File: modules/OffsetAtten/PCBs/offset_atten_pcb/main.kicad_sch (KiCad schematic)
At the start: 25 parts, among them J9 Eurorack_2x5_Power, U1 LM324, U2 LM324

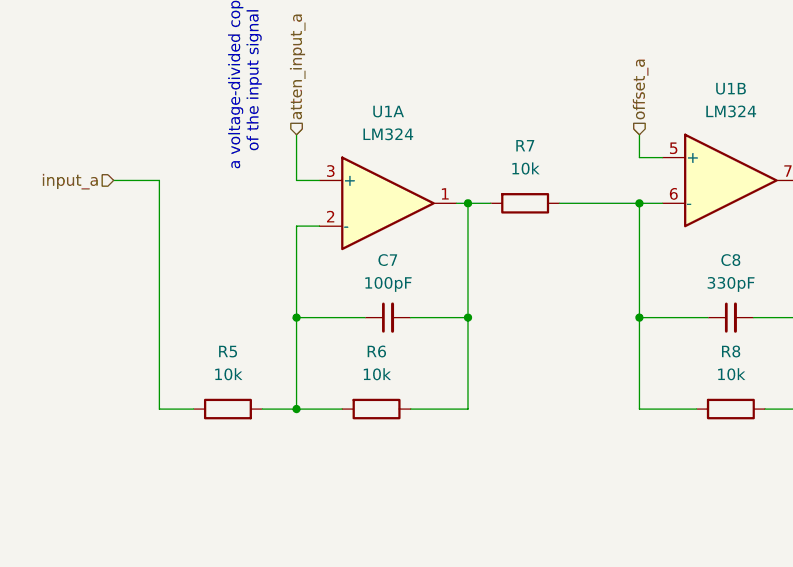
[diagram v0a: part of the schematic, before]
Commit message: Add assembly instructions for O/A
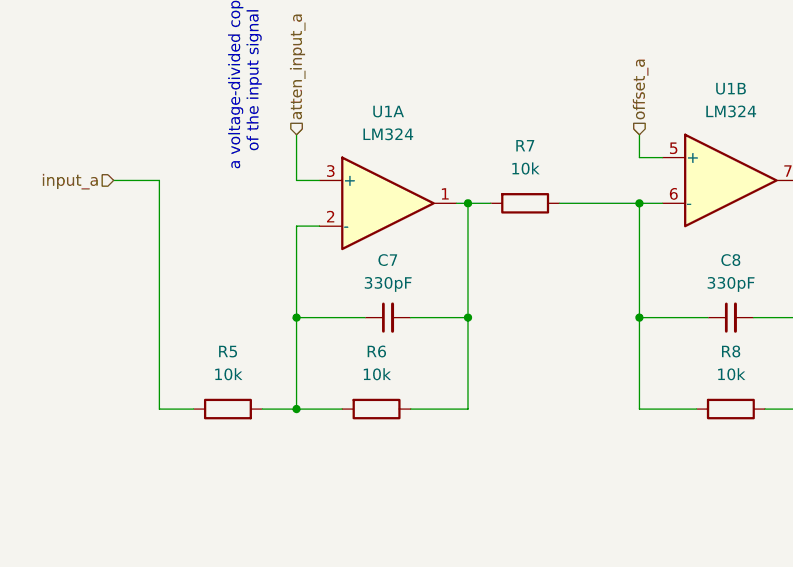
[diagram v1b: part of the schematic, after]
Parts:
- C7: value 100pF -> 330pF
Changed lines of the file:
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@@
 			)
 		)
-		(property "Value" "100pF"
+		(property "Value" "330pF"
 			(at 68.5863 46.99 90)
 			(effects

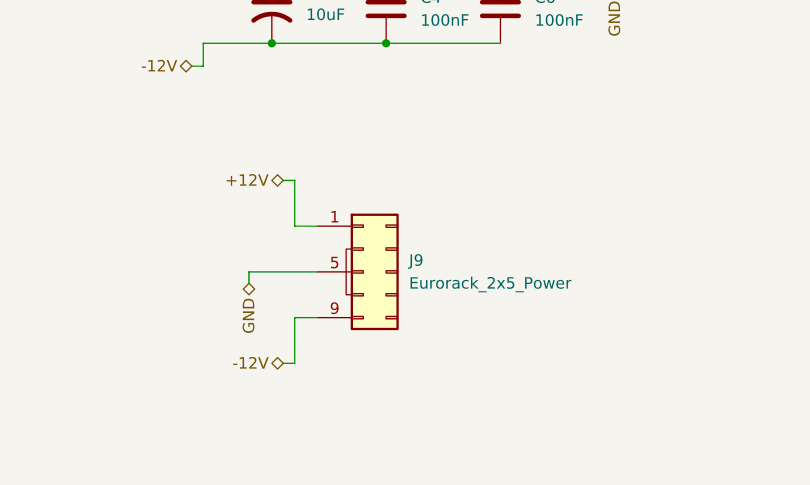
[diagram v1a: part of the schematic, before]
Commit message: Fix O/A power polarity
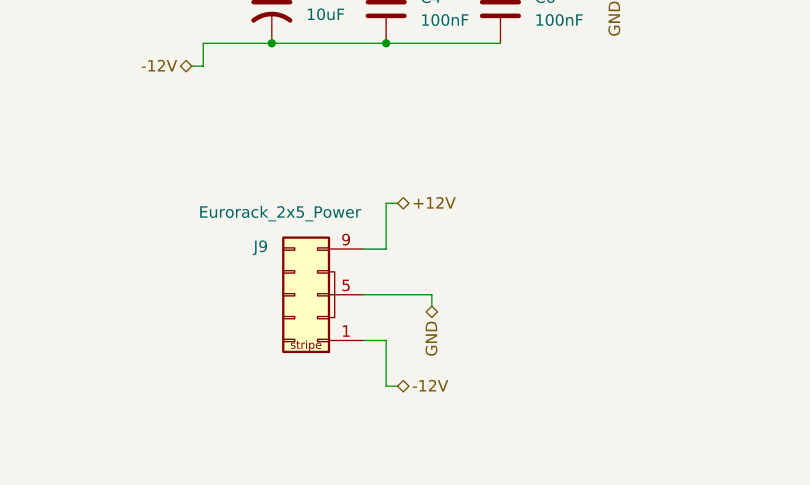
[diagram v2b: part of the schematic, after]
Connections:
- net +12V: now also J9.10 (+12v), J9.9 (+12v); no longer J9.1 (-12v), J9.2 (-12v)
- net -12V: now also J9.1 (-12v), J9.2 (-12v); no longer J9.10 (+12v), J9.9 (+12v)
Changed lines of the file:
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@@
 	(title_block
 		(title "OffsetAtten")
-		(date "2024-04-16")
-		(rev "v0.1")
+		(date "2024-05-01")
+		(rev "v2.0")
 		(company "Free Modular")
 	)
@@
 	(wire
 		(pts
-			(xy 213.36 119.38) (xy 213.36 124.46)
+			(xy 223.52 121.92) (xy 223.52 127)
 		)
 		(stroke
@@
 	(wire
 		(pts
-			(xy 213.36 139.7) (xy 213.36 134.62)
+			(xy 223.52 142.24) (xy 223.52 137.16)
 		)
 		(stroke
@@
 	(wire
 		(pts
-			(xy 208.28 129.54) (xy 208.28 130.81)
+			(xy 228.6 132.08) (xy 228.6 133.35)
 		)
 		(stroke
@@
 	(wire
 		(pts
-			(xy 213.36 134.62) (xy 215.9 134.62)
+			(xy 223.52 137.16) (xy 220.98 137.16)
 		)
 		(stroke
@@
 	(wire
 		(pts
-			(xy 213.36 119.38) (xy 212.09 119.38)
+			(xy 223.52 121.92) (xy 224.79 121.92)
 		)
 		(stroke
@@
 	(wire
 		(pts
-			(xy 213.36 139.7) (xy 212.09 139.7)
+			(xy 223.52 142.24) (xy 224.79 142.24)
 		)
 		(stroke
@@
 	(wire
 		(pts
-			(xy 208.28 129.54) (xy 215.9 129.54)
+			(xy 228.6 132.08) (xy 220.98 132.08)
 		)
 		(stroke
@@
 	(wire
 		(pts
-			(xy 213.36 124.46) (xy 215.9 124.46)
+			(xy 223.52 127) (xy 220.98 127)
 		)
 		(stroke
@@
 	(hierarchical_label "+12V"
 		(shape bidirectional)
-		(at 212.09 119.38 180)
-		(fields_autoplaced yes)
-		(effects
-			(font
-				(size 1.27 1.27)
-			)
-			(justify right)
+		(at 224.79 121.92 0)
+		(fields_autoplaced yes)
+		(effects
+			(font
+				(size 1.27 1.27)
+			)
+			(justify left)
 		)
 	)
@@
 	(hierarchical_label "GND"
 		(shape bidirectional)
-		(at 208.28 130.81 270)
+		(at 228.6 133.35 270)
 		(fields_autoplaced yes)
 		(effects
@@
 	(hierarchical_label "-12V"
 		(shape bidirectional)
-		(at 212.09 139.7 180)
-		(fields_autoplaced yes)
-		(effects
-			(font
-				(size 1.27 1.27)
-			)
-			(justify right)
+		(at 224.79 142.24 0)
+		(fields_autoplaced yes)
+		(effects
+			(font
+				(size 1.27 1.27)
+			)
+			(justify left)
 		)
 	)
@@
 	(symbol
 		(lib_id "FreeModular:Eurorack_2x5_Power")
-		(at 220.98 132.08 0)
+		(at 214.63 132.08 0)
 		(unit 1)
 		(exclude_from_sim no)
@@
 		(on_board yes)
 		(dnp no)
-		(fields_autoplaced yes)
 		(property "Reference" "J9"
-			(at 226.06 128.2699 0)
+			(at 208.788 126.746 0)
 			(effects
 				(font
@@
 		)
 		(property "Value" "Eurorack_2x5_Power"
-			(at 226.06 130.8099 0)
+			(at 202.692 122.936 0)
 			(effects
 				(font
@@
 		)
 		(property "Footprint" "Connector_IDC:IDC-Header_2x05_P2.54mm_Vertical"
-			(at 222.25 139.7 0)
+			(at 215.9 139.7 0)
 			(effects
 				(font
@@
 		)
 		(property "Datasheet" "~"
-			(at 220.98 132.08 0)
+			(at 214.63 132.08 0)
 			(effects
 				(font
@@
 		)
 		(property "Description" "Generic connector, double row, 02x05, odd/even pin numbering scheme (row 1 odd numbers, row 2 even numbers)"
-			(at 220.98 132.08 0)
+			(at 214.63 132.08 0)
 			(effects
 				(font

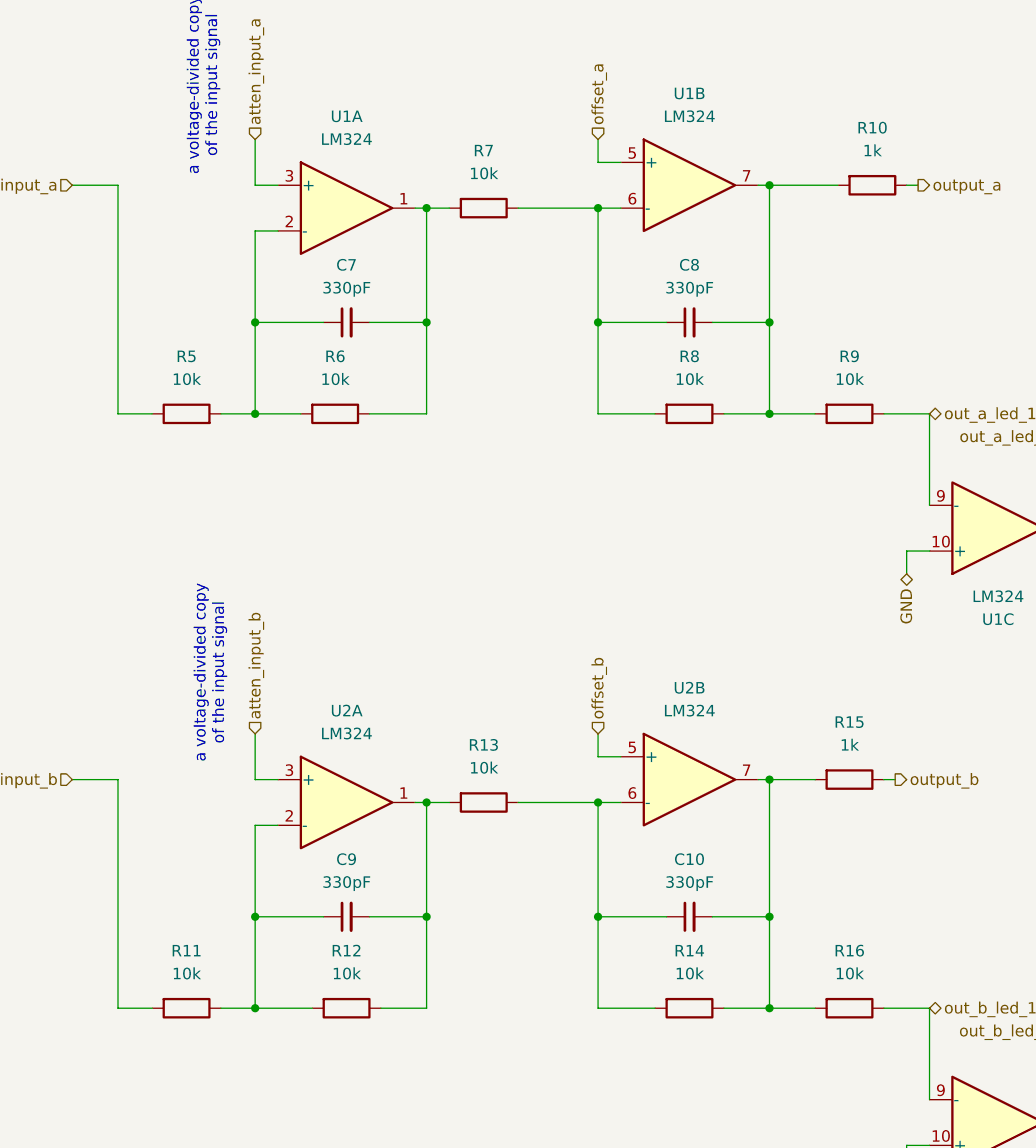
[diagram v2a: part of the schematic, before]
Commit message: Update standoffs in OA PCB
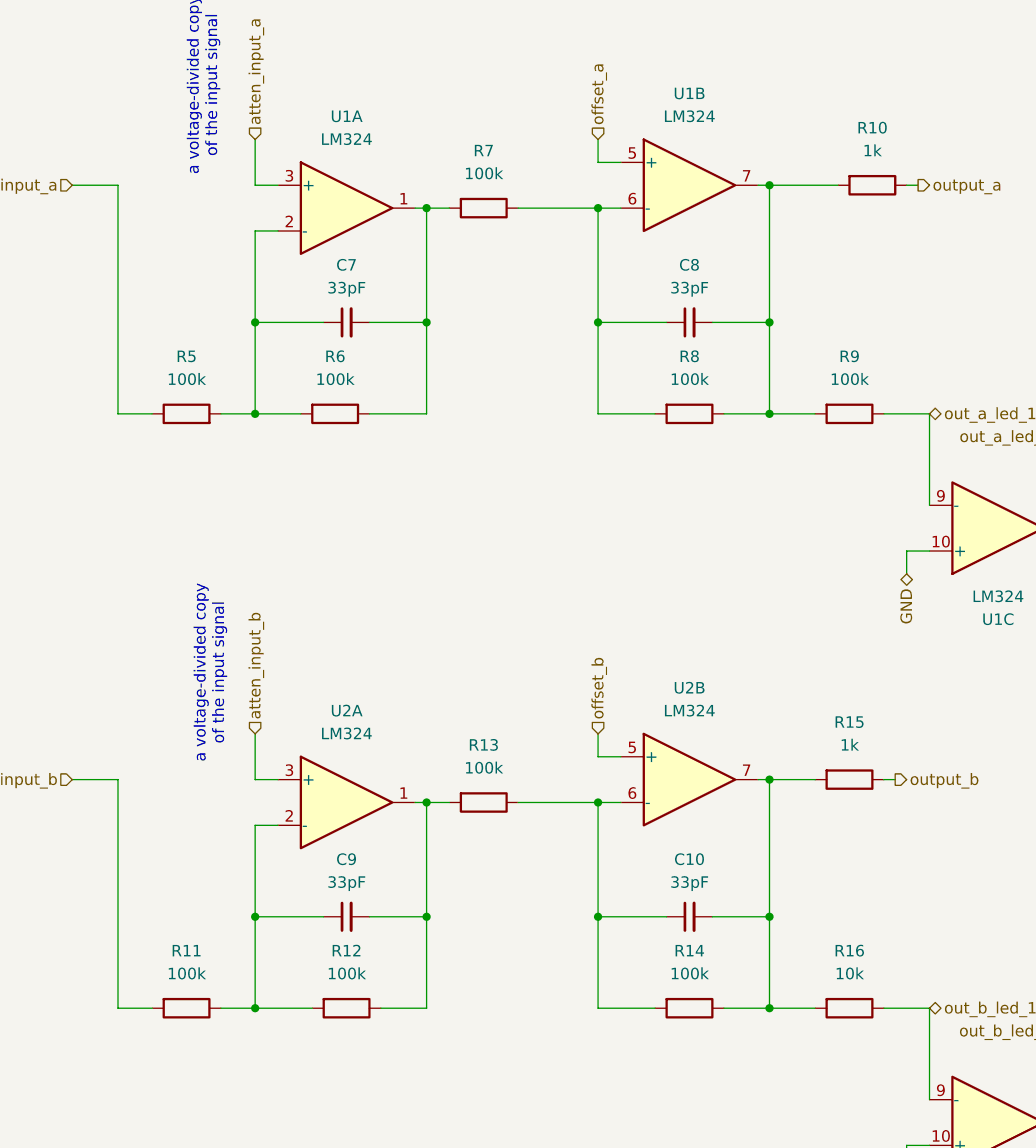
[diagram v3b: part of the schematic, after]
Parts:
- C10, C7, C8, C9: value 330pF -> 33pF
- R11, R12, R13, R14, R5, R6, R7, R8, R9: value 10k -> 100k
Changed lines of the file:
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@@
 			)
 		)
-		(property "Value" "10k"
+		(property "Value" "100k"
 			(at 67.31 57.15 90)
 			(effects
@@
 			)
 		)
-		(property "Value" "10k"
+		(property "Value" "100k"
 			(at 50.8 123.19 90)
 			(effects
@@
 			)
 		)
-		(property "Value" "330pF"
+		(property "Value" "33pF"
 			(at 106.6863 46.99 90)
 			(effects
@@
 			)
 		)
-		(property "Value" "330pF"
+		(property "Value" "33pF"
 			(at 68.5863 46.99 90)
 			(effects
@@
 			)
 		)
-		(property "Value" "330pF"
+		(property "Value" "33pF"
 			(at 68.5863 113.03 90)
 			(effects
@@
 			)
 		)
-		(property "Value" "10k"
+		(property "Value" "100k"
 			(at 50.8 57.15 90)
 			(effects
@@
 			)
 		)
-		(property "Value" "10k"
+		(property "Value" "100k"
 			(at 106.68 57.15 90)
 			(effects
@@
 			)
 		)
-		(property "Value" "10k"
+		(property "Value" "100k"
 			(at 106.68 123.19 90)
 			(effects
@@
 			)
 		)
-		(property "Value" "10k"
+		(property "Value" "100k"
 			(at 83.82 34.29 90)
 			(effects
@@
 			)
 		)
-		(property "Value" "10k"
+		(property "Value" "100k"
 			(at 124.46 57.15 90)
 			(effects
@@
 			)
 		)
-		(property "Value" "10k"
+		(property "Value" "100k"
 			(at 83.82 100.33 90)
 			(effects
@@
 			)
 		)
-		(property "Value" "330pF"
+		(property "Value" "33pF"
 			(at 106.6863 113.03 90)
 			(effects
@@
 			)
 		)
-		(property "Value" "10k"
+		(property "Value" "100k"
 			(at 68.58 123.19 90)
 			(effects

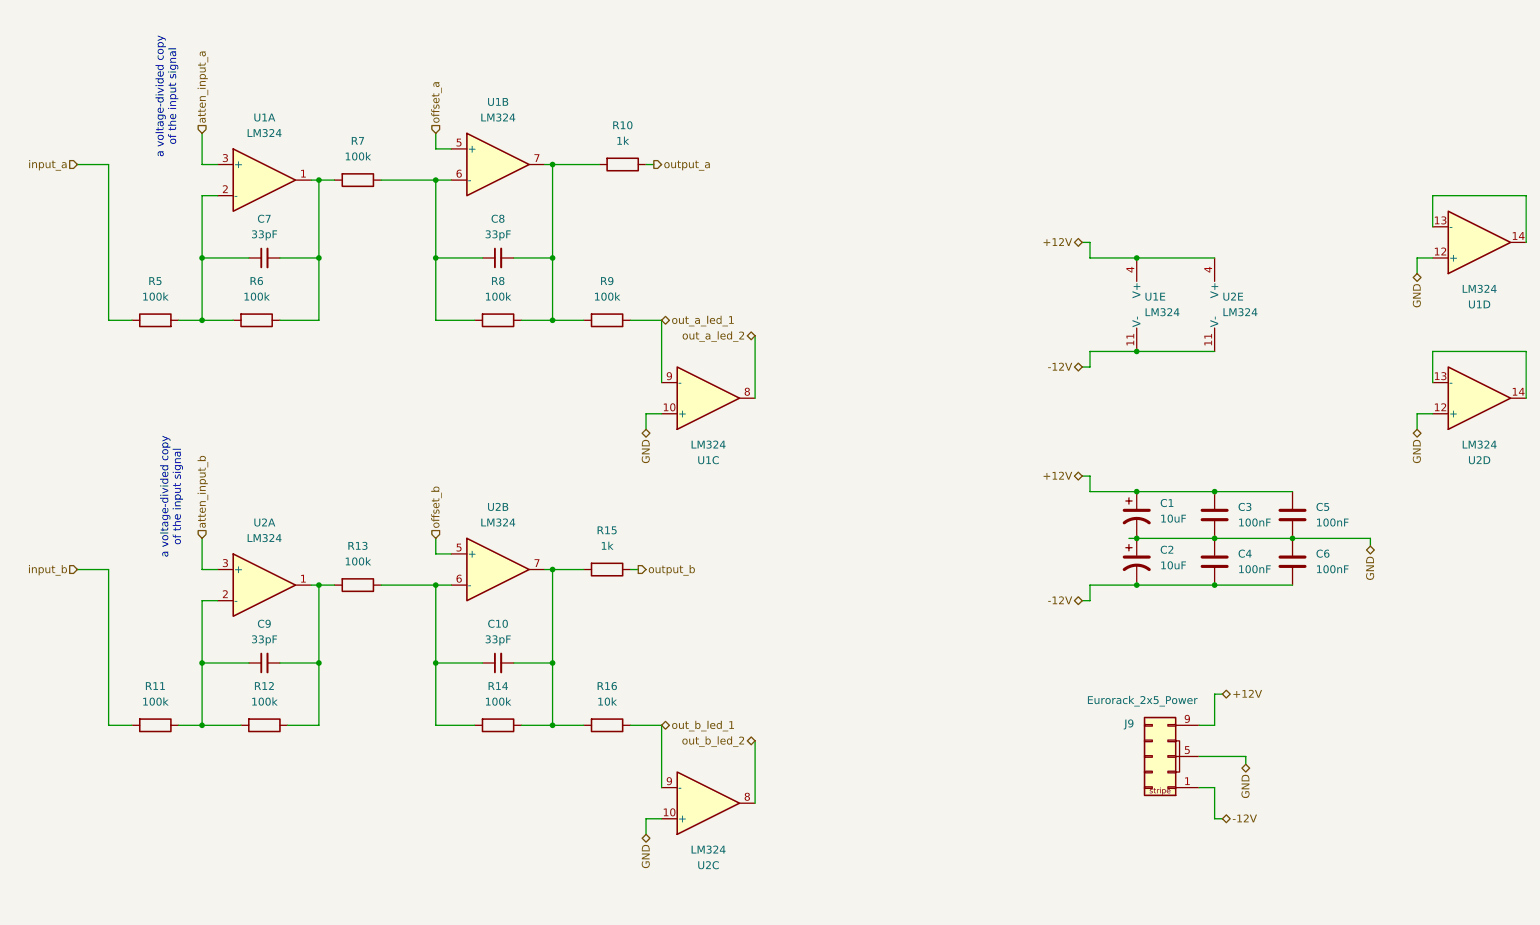
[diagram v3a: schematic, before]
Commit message: Add buffer to O/A; (see #67) closes #62
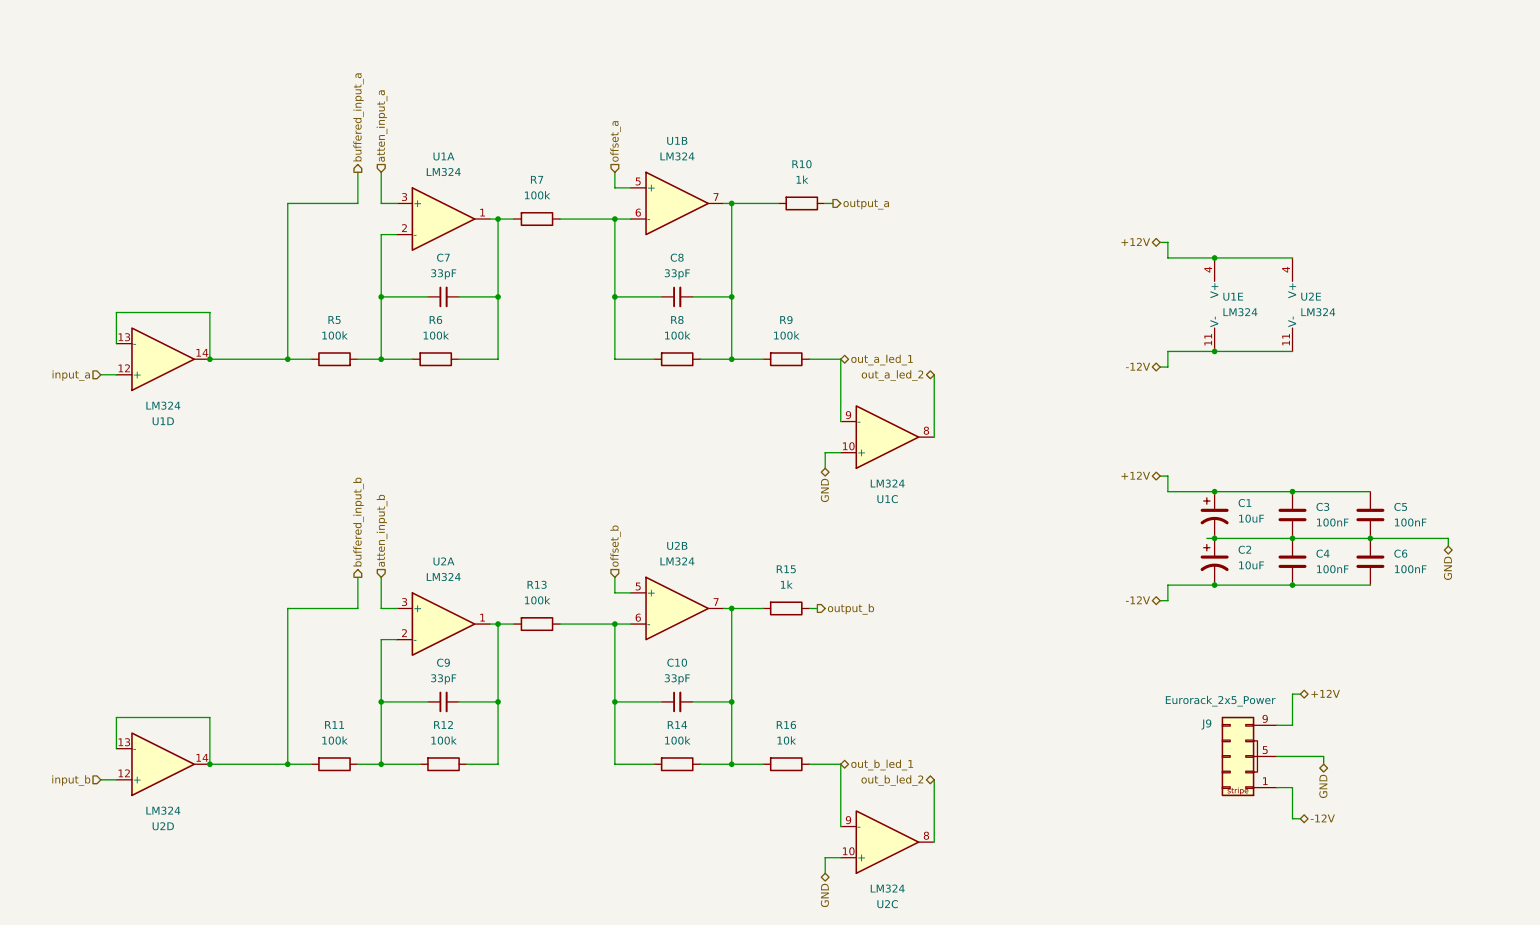
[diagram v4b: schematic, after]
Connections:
- net GND: no longer U1.12 (+), U2.12 (+)
- net input_a: now also U1.12 (+); no longer R5.1
- net input_b: now also U2.12 (+); no longer R11.2
- net buffered_input_a: now reaches U1.13 (-), U1.14
- net buffered_input_a: now also R5.1
- net buffered_input_b: now reaches U2.13 (-), U2.14
- net buffered_input_b: now also R11.2
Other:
- note removed: "a voltage-divided copy of the input signal"
- moved on the sheet: C1, C10, C2, C3, C4, C5, C6, C7, C8, C9, J9, R10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

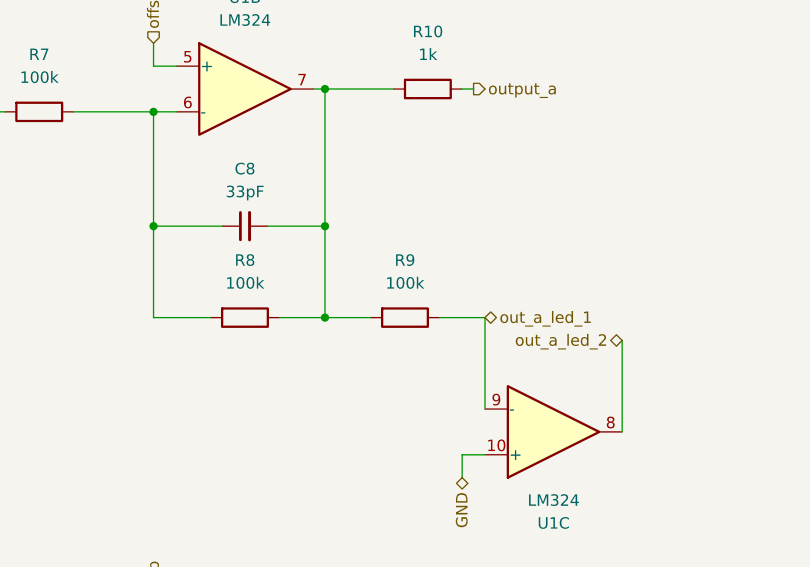
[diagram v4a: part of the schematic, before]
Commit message: Fix O/A typo
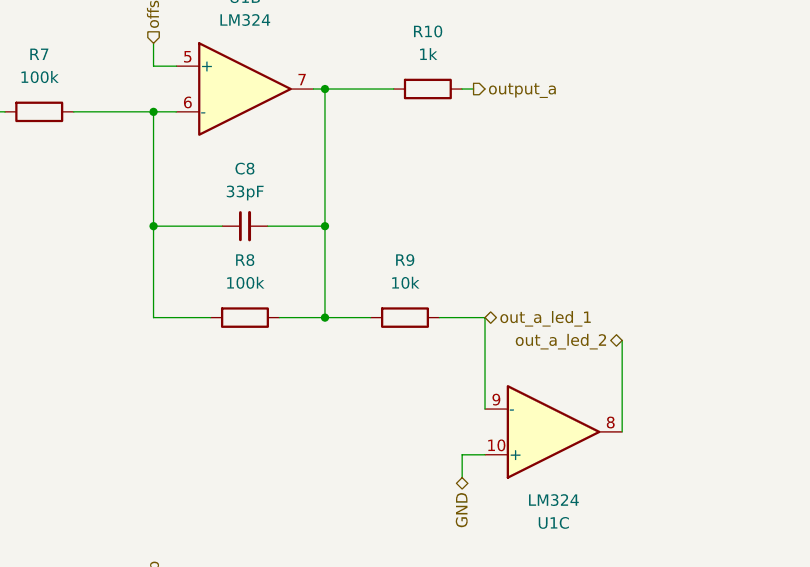
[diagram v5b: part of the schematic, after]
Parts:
- R9: value 100k -> 10k
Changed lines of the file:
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@@
 			)
 		)
-		(property "Value" "100k"
+		(property "Value" "10k"
 			(at 153.67 63.5 90)
 			(effects
